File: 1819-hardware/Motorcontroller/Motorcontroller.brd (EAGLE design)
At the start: 44.8 x 54 mm, 36 parts, among them U1 MAX3485CSA, U3 PCA9306, U4 74HC1G04

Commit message: started motorcontroller board files
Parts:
- removed B2: Pressure Sensor, SparkFun-Boards:SPARKFUN_MS5803-14BA_BREAKOUT
- removed J1: (no value), SparkFun-Connectors:1X04_NO_SILK
- removed R15, R17: 4.7k, SparkFun-Resistors:0603
- removed R16: 100k, SparkFun-Resistors:0603
- removed U4: 74HC1G04, SparkFun-IC-Logic:SOT353
- added C8: 10uF, SparkFun-Capacitors:CPOL-RADIAL-2.5MM-5MM
- added J6: (no value), SparkFun-Connectors:1X08_LONGPADS
- added U2: GENERIC-SOIC8MSGEQ7N-FILTER, SparkFun-Retired:SO08
- C2, C5: value 0.1uF -> 10uF; device SparkFun-Capacitors:0603 -> SparkFun-Capacitors:CPOL-RADIAL-2.5MM-5MM
- C3: value 10uF -> 0.1uF; device SparkFun-Capacitors:CPOL-RADIAL-2.5MM-5MM -> SparkFun-Capacitors:0603
- J2: device SparkFun-Connectors:1X06_NO_SILK -> SparkFun-Connectors:1X01_NO_SILK
- J3: device SparkFun-Connectors:1X02 -> SparkFun-Connectors:1X01_NO_SILK
- J5: device SparkFun-Connectors:1X03 -> SparkFun-Connectors:1X01_NO_SILK
- R1: value 100 -> 4.7k
- R13: value 100k -> 47k
- R14: value 4.7k -> 47k
- R4: value 680 -> 4.7k
- R9: value 680 -> 47k
- U1: value MAX3485CSA -> GENERIC-SOIC8MSGEQ7N-FILTER; device SparkFun-IC-Comms:SO08 -> SparkFun-Retired:SO08
- U3: value PCA9306 -> GENERIC-SOIC8MSGEQ7N-FILTER; device SparkFun-IC-Comms:PSOP-8 -> SparkFun-Retired:SO08
- moved FRAME1 121.6 mm to (-80.0, 47.0)
- moved R3 48.7 mm to (3.81, 43.2), turned to 180 degrees
- moved J4 48.1 mm to (10.2, 47.0), turned to 180 degrees
- moved R6 45.8 mm to (3.81, 41.3), turned to 0 degrees
- moved R7 43.1 mm to (3.81, 39.4), turned to 0 degrees
- moved R2 42.9 mm to (8.89, 43.2), turned to 0 degrees
- moved R5 39.6 mm to (8.89, 41.3), turned to 180 degrees
- moved R8 36.5 mm to (8.89, 39.4), turned to 180 degrees
- moved C6 36.0 mm to (15.2, 41.3)
- moved J5 35.9 mm to (28.6, 27.9)
- moved C2 34.3 mm to (28.6, 34.3), flipped to the top
- moved U$1 31.4 mm to (24.1, 40.0), turned to 90 degrees
- moved U1 29.2 mm to (28.6, 3.81), flipped to the top, turned to 90 degrees
- moved R11 27.7 mm to (3.81, 40.6), turned to 0 degrees
- moved C1 25.8 mm to (15.2, 39.4)
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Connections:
- removed net 3V3: B2.3.3V, J2.2, U3.1
- removed net 485A: J3.1, R1.1, R4.2, U1.6
- removed net 485B: J3.2, R1.2, R9.1, U1.7
- removed net N$19: C5.1, R13.1, U3.7, U3.8
- removed net RESET: B1.13, B1.3
- removed net RX: B1.2, U1.1
- removed net SCL3V3: B2.SCL/SCLK, U3.2
- removed net SDA3V3: B2.SDA/SDI, U3.3
- removed net TX: B1.1, U1.4, U4.2
- removed net VOLTAGE_SENSOR: B1.17, R16.1, R17.2
- new net M1DIR1: J6.3
- new net M1DIR2: J6.4
- new net M1IN1: B1.6, U1.3
- new net M1IN2: B1.8, U1.2
- new net M1OUT1: U1.6
- new net M1OUT2: U1.8
- new net M2DIR1: J6.5
- new net M2DIR2: J6.6
- new net M2IN1: B1.9, U2.3
- new net M2IN2: B1.12, U2.2
- new net M2OUT1: U2.6
- new net M2OUT2: U2.8
- new net M3DIR1: J6.7
- new net M3DIR2: J6.8
- new net M3IN1: B1.13, U3.3
- new net M3IN2: B1.14, U3.2
- new net M3OUT1: U3.6
- new net M3OUT2: U3.8
- new net N$2: R14.2, U3.4
- new net N$7: R9.2, U1.4
- net 12V: no longer J5.2
- net BATT: now also C2.1, C5.1, C8.1, J6.2, U1.5, U2.5, U3.5; no longer J5.3, R16.2
- net BLUE: now also B1.16; no longer B1.14
- net GND: now also C8.2, J2.1, J3.1, J6.1, R13.1, R14.1, R9.1, U1.1, U1.7, U2.1, U2.7, U3.1, U3.7; no longer B2.GND, J2.3, R17.1, R4.1, U1.5, U3.4, U4.3
- net N$1: now also R13.2, U2.4; no longer U1.2, U1.3, U4.4
- net RED: now also B1.11; no longer B1.16
- net SCL: now also R1.1; no longer J2.5, R14.2, U3.6
- net SDA: now also R4.1; no longer J2.4, R15.2, U3.5
- net VCC: now also R1.2, R4.2; no longer C2.1, J2.1, R13.2, R14.1, R15.1, R9.2, U1.8, U4.5
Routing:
- net SCL: track 54.9 -> 0.00 mm, vias 3 -> 0
- net SDA: track 51.1 -> 0.00 mm, vias 1 -> 0
- net 3V3: track 31.7 -> 0.00 mm, vias 1 -> 0
- net VOLTAGE_SENSOR: track 31.0 -> 0.00 mm, vias 2 -> 0
- net TX: track 27.5 -> 0.00 mm
- net 485A: track 27.1 -> 0.00 mm
- net 485B: track 24.9 -> 0.00 mm
- net RX: track 20.4 -> 0.00 mm
- net SDA-: track 15.5 -> 0.00 mm
- net SCL-: track 13.7 -> 0.00 mm
- net SDA+: track 13.6 -> 0.00 mm
- net SCL+: track 13.4 -> 0.00 mm
- net VCC: track 11.9 -> 0.00 mm
- net 12V: track 9.93 -> 0.00 mm
- net SDA3V3: track 8.90 -> 0.00 mm
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- removed copper zone on layer 16, net GND
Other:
- board size 44.8 x 54 mm -> 34.3 x 50.6 mm
- board text removed: "AUTOPILOT BOARD TJROV ELECTRICAL, 2018"
- board text removed: "STATUS YELLOW: DISCONNECTED GREEN SOLID: DISARMED GREEN FLASH: ARMED RED: ERROR"

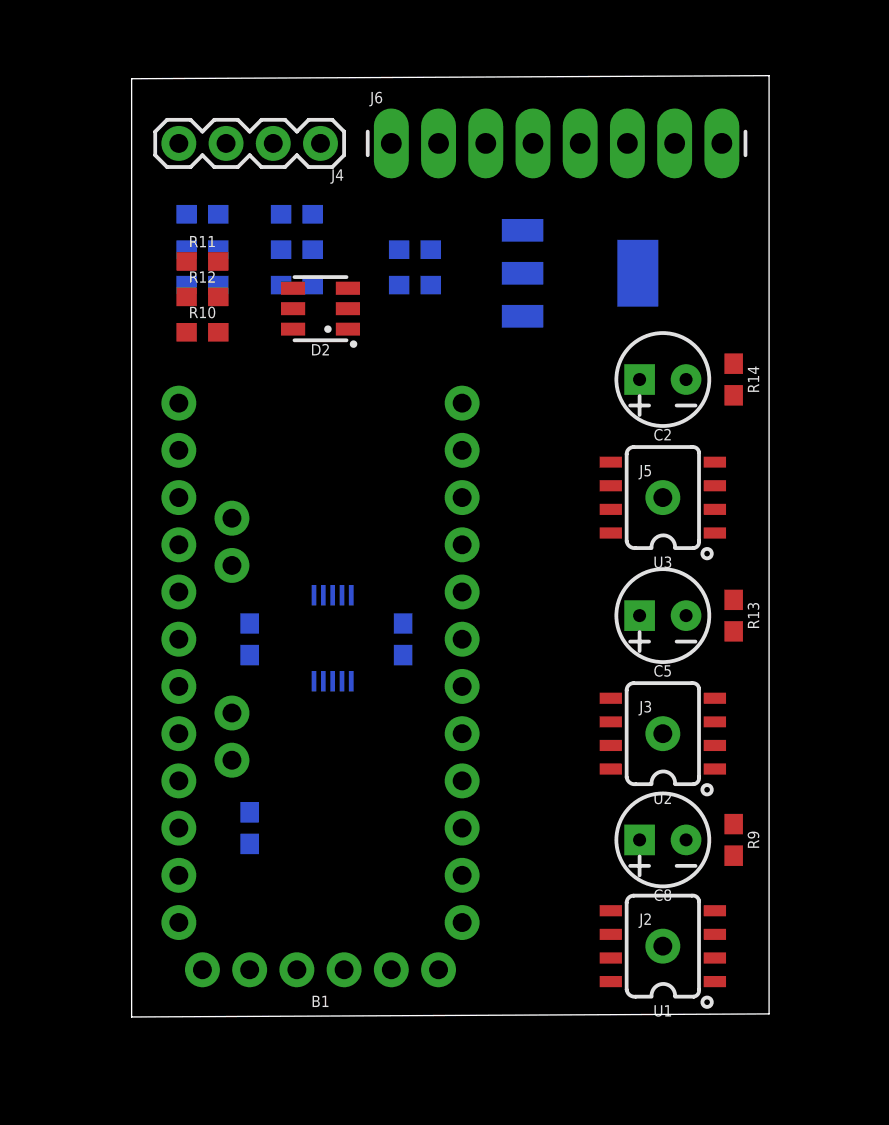
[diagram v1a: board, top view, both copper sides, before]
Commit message: routing of motorcontroller board files
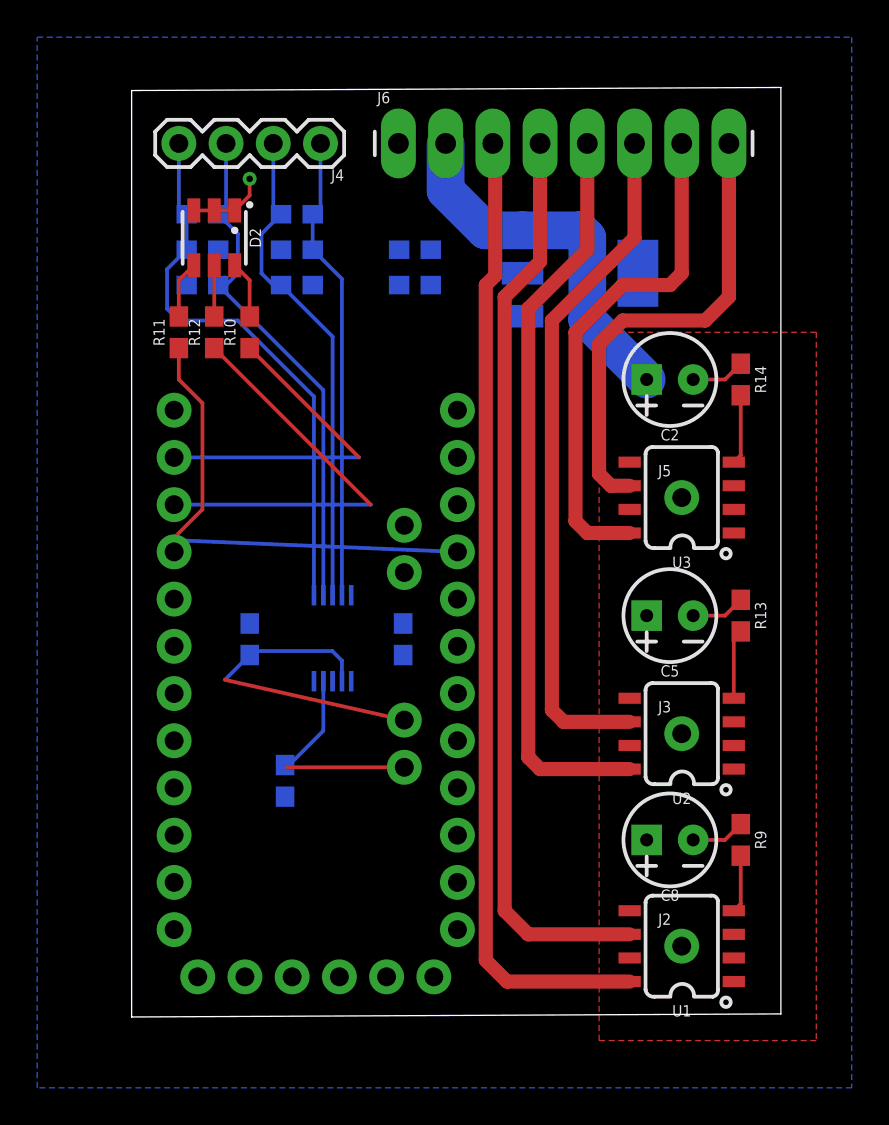
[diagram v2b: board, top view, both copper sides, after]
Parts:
- moved D2 6.87 mm to (4.45, 41.9), turned to 270 degrees
- moved R11 4.02 mm to (2.54, 36.8), turned to 90 degrees
- moved R1 3.18 mm to (8.26, 12.7)
- moved R10 2.54 mm to (6.35, 36.8), turned to 90 degrees
- moved R12 2.01 mm to (4.45, 36.8), turned to 90 degrees
- moved J2 1.02 mm to (29.6, 3.81)
- moved J3 1.02 mm to (29.6, 15.2)
- moved J5 1.02 mm to (29.6, 27.9)
- moved U1 1.02 mm to (29.6, 3.81)
- moved U2 1.02 mm to (29.6, 15.2)
- moved U3 1.02 mm to (29.6, 27.9)
- moved B1 0.46 mm to (9.91, 17.4), flipped to the bottom
- moved C2 0.38 mm to (29.0, 34.3)
- moved C5 0.38 mm to (29.0, 21.6)
- moved C8 0.38 mm to (29.0, 9.53)
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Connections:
- removed net 12V: C6.1, U$1.3
- removed net M1DIR1: J6.3
- removed net M1DIR2: J6.4
- removed net M2DIR1: J6.5
- removed net M2DIR2: J6.6
- removed net M3DIR1: J6.7
- removed net M3DIR2: J6.8
- net BATT: now also C6.1, U$1.3
- net GREEN: now also B1.10; no longer B1.15
- net M1OUT1: now also J6.4
- net M1OUT2: now also J6.3
- net M2OUT1: now also J6.6
- net M2OUT2: now also J6.5
- net M3OUT1: now also J6.8
- net M3OUT2: now also J6.7
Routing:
- net M1OUT2: track 0.00 -> 52.4 mm
- net M1OUT1: track 0.00 -> 49.3 mm
- net M2OUT2: track 0.00 -> 40.1 mm
- net M2OUT1: track 0.00 -> 36.8 mm
- net SCL-: track 0.00 -> 30.0 mm
- net SCL+: track 0.00 -> 27.9 mm
- net M3OUT2: track 0.00 -> 27.4 mm
- net BLUE: track 0.00 -> 26.9 mm
- net SDA+: track 0.00 -> 26.7 mm
- net M3OUT1: track 0.00 -> 25.2 mm
- net SDA-: track 0.00 -> 25.1 mm
- net GREEN: track 0.00 -> 22.5 mm
- net BATT: track 0.00 -> 20.2 mm
- net RED: track 0.00 -> 18.3 mm
- net SDA: track 0.00 -> 18.2 mm
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- added copper zone on layer 1, net BATT
- added copper zone on layer 16, net GND
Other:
- board size 34.3 x 50.6 mm -> 34.9 x 50 mm

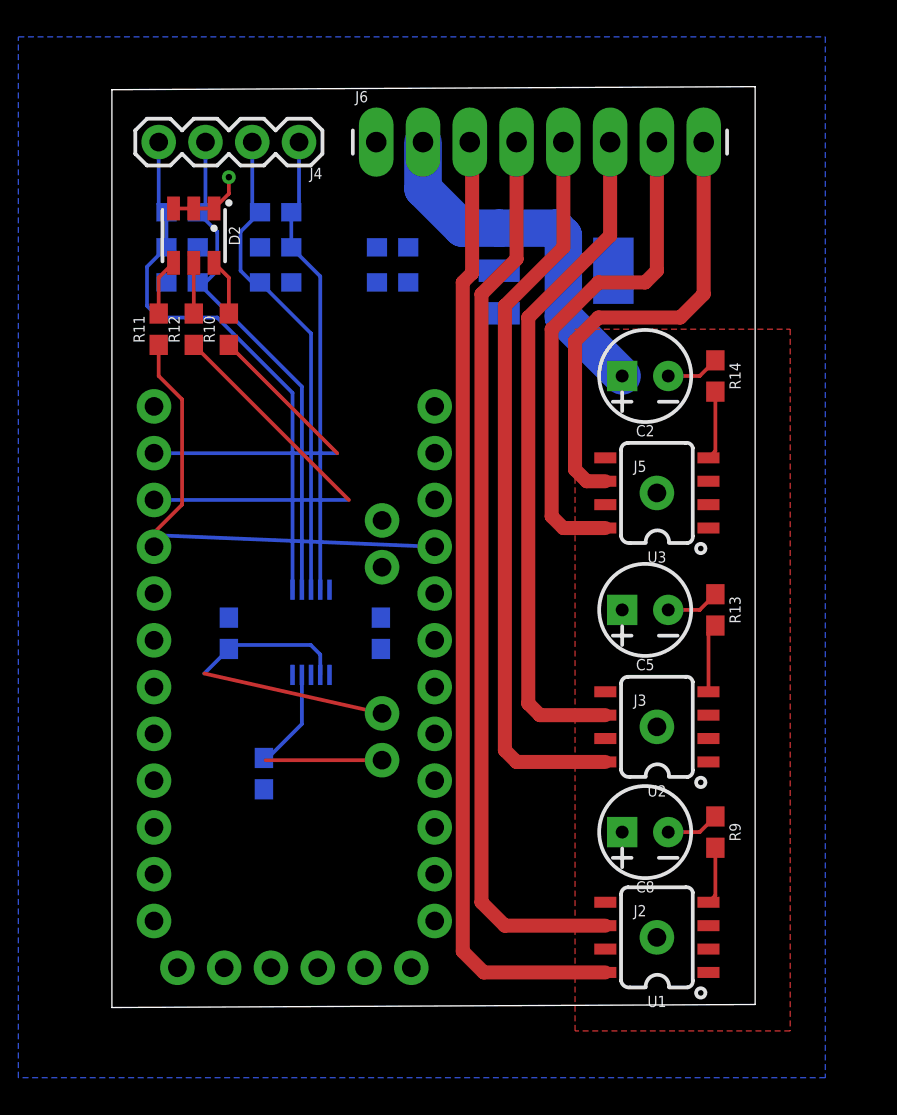
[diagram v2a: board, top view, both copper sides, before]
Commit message: more board routing
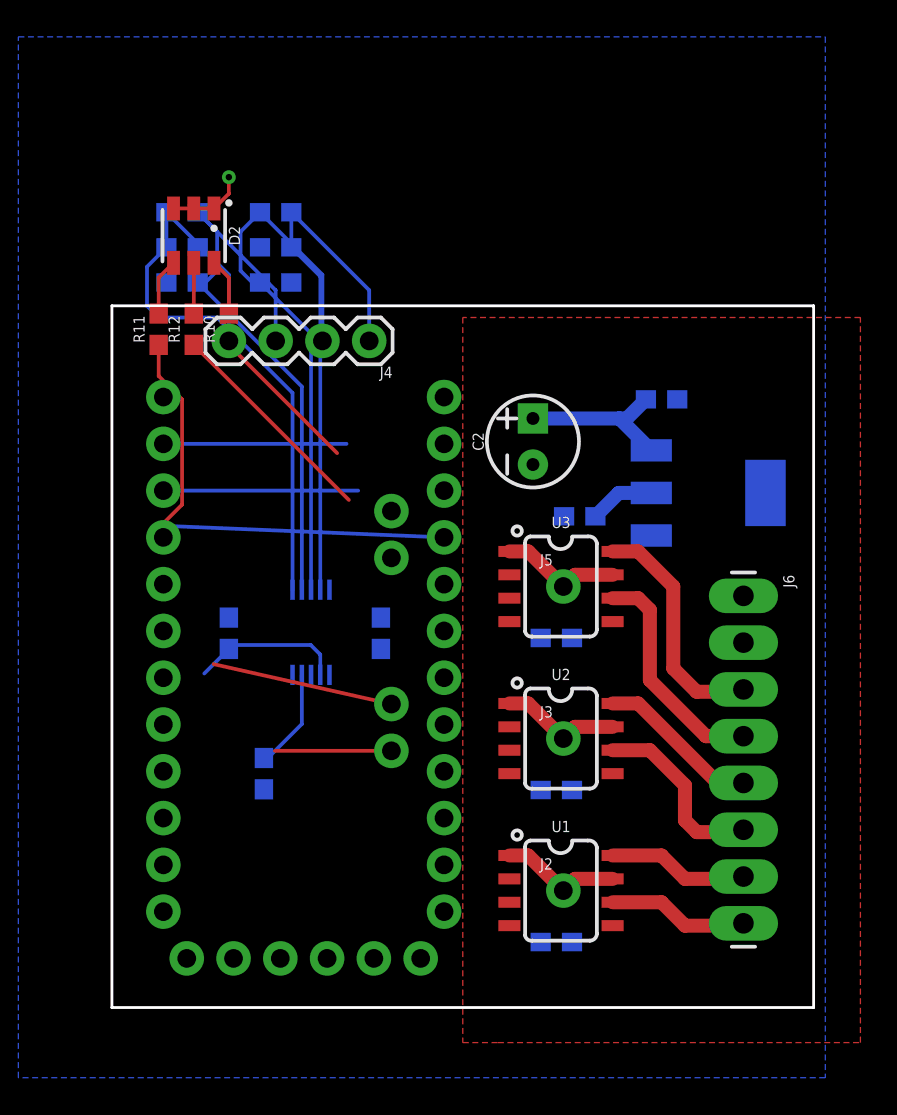
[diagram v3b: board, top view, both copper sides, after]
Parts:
- removed C5, C8: 10uF, SparkFun-Capacitors:CPOL-RADIAL-2.5MM-5MM
- moved J6 31.7 mm to (34.3, 22.4), turned to 270 degrees
- moved C6 16.8 mm to (29.8, 33.0), turned to 180 degrees
- moved R14 16.6 mm to (24.1, 20.1), flipped to the bottom, turned to 0 degrees
- moved C1 16.3 mm to (25.4, 26.7)
- moved U$1 14.6 mm to (32.4, 27.9)
- moved R13 13.0 mm to (24.1, 11.8), flipped to the bottom, turned to 0 degrees
- moved J4 11.4 mm to (14.0, 36.2)
- moved R9 10.5 mm to (24.1, 3.56), flipped to the bottom, turned to 0 degrees
- moved U3 7.27 mm to (24.4, 22.9), turned to 270 degrees
- moved J5 7.18 mm to (24.5, 22.9)
- moved C2 7.06 mm to (22.9, 30.7), turned to 90 degrees
- moved U1 5.79 mm to (24.4, 6.35), turned to 270 degrees
- moved J2 5.68 mm to (24.5, 6.35)
- moved U2 5.25 mm to (24.4, 14.6), turned to 270 degrees
- moved J3 5.12 mm to (24.5, 14.6)
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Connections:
- net BATT: no longer C5.1, C8.1
- net GND: no longer C5.2, C8.2
- net M1OUT1: now also J6.8; no longer J6.4
- net M1OUT2: now also J6.7; no longer J6.3
- net M3IN1: now also B1.14; no longer B1.13
- net M3IN2: now also B1.13; no longer B1.14
- net M3OUT1: now also J6.4; no longer J6.8
- net M3OUT2: now also J6.3; no longer J6.7
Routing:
- net M1OUT2: track 52.4 -> 7.68 mm
- net M1OUT1: track 49.3 -> 7.68 mm
- net M2OUT2: track 40.1 -> 8.89 mm
- net M2OUT1: track 36.8 -> 10.1 mm
- net M3OUT2: track 27.4 -> 12.9 mm
- net M3OUT1: track 25.2 -> 12.4 mm
- net GND: track 13.0 -> 24.2 mm
- net BATT: track 20.2 -> 9.01 mm
- net SDA-: track 25.1 -> 29.9 mm
- net SCL+: track 27.9 -> 32.7 mm
- net SDA+: track 26.7 -> 31.2 mm
- net SCL-: track 30.0 -> 34.5 mm
- net N$2: track 3.75 -> 0.00 mm
- net N$1: track 3.75 -> 0.00 mm
- net VCC: track 0.00 -> 3.56 mm
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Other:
- board size 34.9 x 50 mm -> 38.1 x 38.1 mm

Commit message: working on motorcontroller board files
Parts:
- moved D2 30.8 mm to (34.3, 34.3), turned to 180 degrees
- moved R11 27.3 mm to (29.8, 35.6), turned to 0 degrees
- moved R12 25.6 mm to (29.8, 33.7), turned to 0 degrees
- moved R10 24.0 mm to (29.8, 31.8), turned to 0 degrees
- moved R5 10.9 mm to (12.7, 31.1)
- moved R6 10.9 mm to (7.62, 31.1)
- moved R2 10.9 mm to (12.7, 33.0)
- moved R3 10.9 mm to (7.62, 33.0)
- moved R7 10.9 mm to (7.62, 29.2)
- moved R8 10.9 mm to (12.7, 29.2)
- moved R4 8.26 mm to (14.6, 20.3)
- moved C3 7.62 mm to (6.99, 20.3)
- moved R1 6.84 mm to (14.6, 10.2)
- moved R9 1.27 mm to (24.1, 2.29)
- moved R13 1.27 mm to (24.1, 10.5)
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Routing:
- net BLUE: track 26.9 -> 0.00 mm
- net GREEN: track 22.5 -> 0.00 mm
- net VCC: track 3.56 -> 22.4 mm
- net RED: track 18.3 -> 0.00 mm
- net SCL+: track 32.7 -> 15.6 mm
- net SCL-: track 34.5 -> 17.7 mm
- net SDA+: track 31.2 -> 15.0 mm
- net SDA-: track 29.9 -> 15.5 mm
- net SDA: track 18.2 -> 8.22 mm
- net N$7: track 0.00 -> 4.16 mm, vias 0 -> 1
- net N$2: track 0.00 -> 4.16 mm, vias 0 -> 1
- net N$1: track 0.00 -> 4.16 mm, vias 0 -> 1
- net N$5: track 3.09 -> 0.00 mm
- net N$4: track 3.09 -> 0.00 mm
- net N$6: track 2.76 -> 0.00 mm
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
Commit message: worked on routing
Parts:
- added J1, J7, J8: (no value), SparkFun-Connectors:1X01_NO_SILK
- FRAME1: value FRAME-LETTER -> FRAME-LETTERNO_PACKAGE; device SparkFun-Aesthetics:CREATIVE_COMMONS -> SparkFun-Aesthetics:DUMMY
- moved C1 8.89 mm to (34.3, 26.7), turned to 180 degrees
- moved C6 7.73 mm to (31.1, 25.4), turned to 270 degrees
- moved U$1 4.49 mm to (33.0, 32.4), turned to 0 degrees
- moved C2 3.75 mm to (26.3, 29.2), turned to 0 degrees
- moved R10 0.63 mm to (29.2, 31.8)
- moved R11 0.63 mm to (29.2, 35.6)
- moved R12 0.63 mm to (29.2, 33.7)
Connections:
- net BATT: now also J1.1, J7.1, J8.1
- net GREEN: now also B1.17; no longer B1.10
- net RED: now also B1.18; no longer B1.11
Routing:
- net M2IN2: track 0.00 -> 27.3 mm
- net M1IN2: track 0.00 -> 26.6 mm
- net M1IN1: track 0.00 -> 24.4 mm
- net M2IN1: track 0.00 -> 24.3 mm
- net VCC: track 22.4 -> 43.2 mm, vias 0 -> 4
- net RED: track 0.00 -> 19.8 mm, vias 0 -> 1
- net GREEN: track 0.00 -> 19.3 mm, vias 0 -> 1
- net BLUE: track 0.00 -> 18.3 mm, vias 0 -> 1
- net M3IN2: track 0.00 -> 12.8 mm
- net M3IN1: track 0.00 -> 11.5 mm
- net GND: track 22.2 -> 28.8 mm, vias 0 -> 5
- net BATT: track 9.01 -> 12.8 mm
- net N$4: track 0.00 -> 3.35 mm
- net N$6: track 0.00 -> 3.02 mm
- net N$5: track 0.00 -> 2.83 mm
- added copper zone on layer 16, net BATT
- added copper zone on layer 1, net VCC
- removed copper zone on layer 1, net BATT
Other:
- board text added: "MOTOR CONTROL BOARD TJROV 2018"
- board text added: "STATUS"
